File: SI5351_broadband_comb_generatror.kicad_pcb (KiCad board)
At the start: 4 copper layers, 142 x 75 mm, 129 parts, among them J1 Conn_Coaxial_Small, J10 Conn_01x06_Socket, J11 RFShield_TwoPieces, J2 RFShield_TwoPieces, J3 Barrel_Jack_Switch, J4 Conn_Coaxial_Small, J5 Conn_01x10_Pin, J6 Conn_01x06_Socket, J7 USB_B, J8 AVR-ISP-6, J9 Conn_Coaxial_Small, SW1 SW_SP5T_NR01105, U1 ISL3280ExHZ, U10 ATmega328PB-A, U11 FT232RL, U12 WE-TVS-82400102, U2 PHA-13HLN+, U3 GAT-10+, U4 GAT-10+, U5 Si5351C-B-GM, U6 PHA-13HLN+, U8 AMS1117-3.3, U9 L7809, Y1 ECS-2520MV-xxx-xx, Y2 TG2520SMN-xx.xxxxxxMhz-xxxxNM

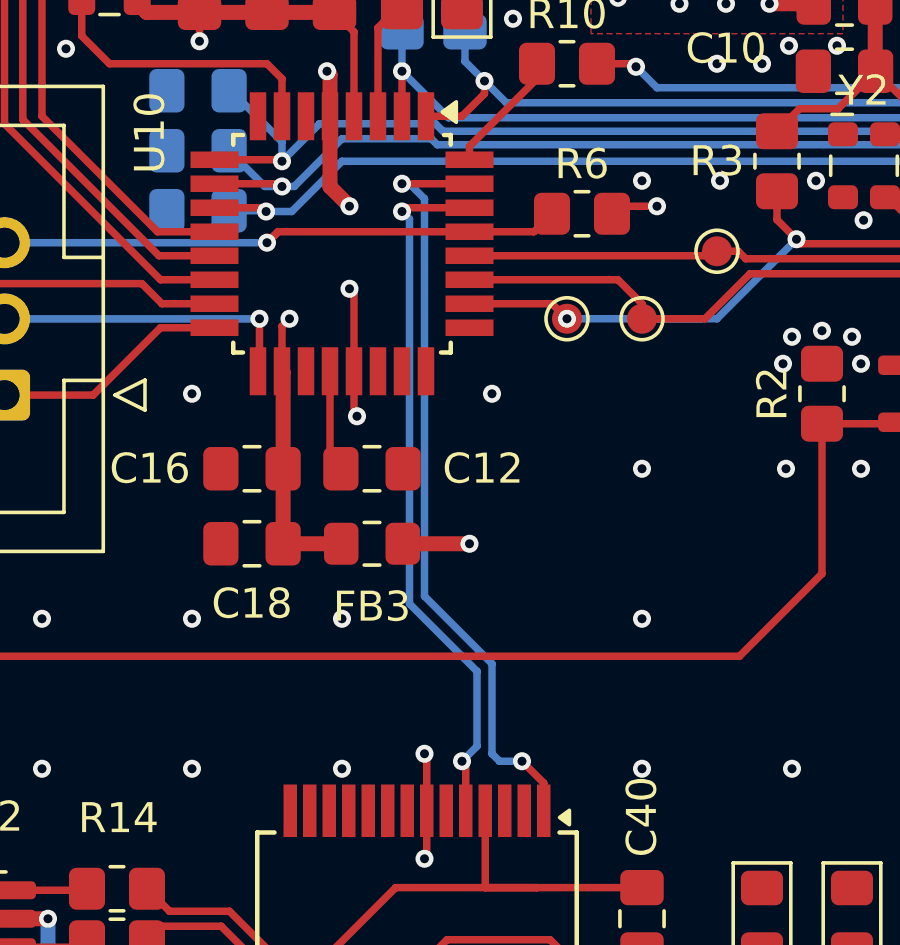
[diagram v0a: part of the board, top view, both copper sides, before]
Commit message: Der Klassiker: RX und TX Leitungen vertauscht. Jetzt im Dutzend billiger. Korrigiert...
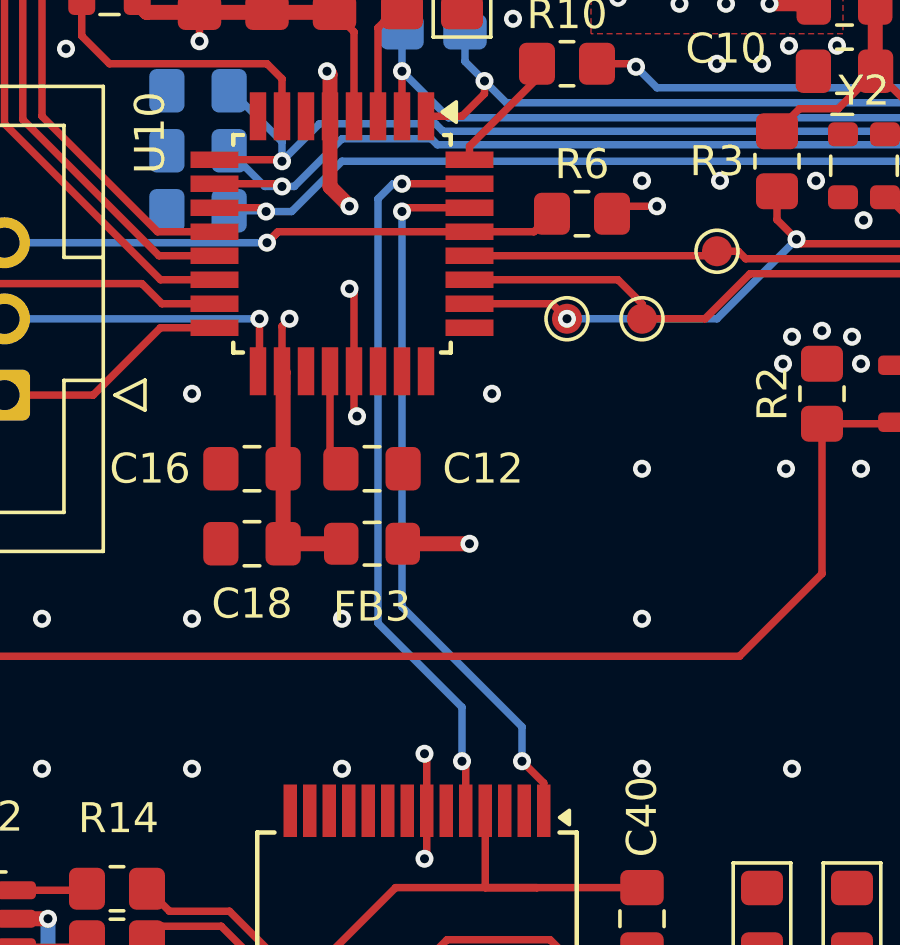
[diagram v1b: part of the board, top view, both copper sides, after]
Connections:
- U11 pad 1: /Controller/TXD -> /Controller/RXD
- U11 pad 5: /Controller/RXD -> /Controller/TXD
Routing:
- net /Controller/TXD: track 25.7 -> 24.9 mm
- net /Controller/RXD: track 23.6 -> 24.2 mm
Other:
- board text added: "SI5351 Kammgenerator rev 1.1 Professur für TET und EMV, TU Dresden 2025 DM2LCT"
- board text removed: "SI5351 Kammgenerator Professur für TET und EMV, TU Dresden 2025 DM2LCT"
